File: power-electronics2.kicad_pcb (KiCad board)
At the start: 2 copper layers, 2 parts, among them U1 STP16NF06

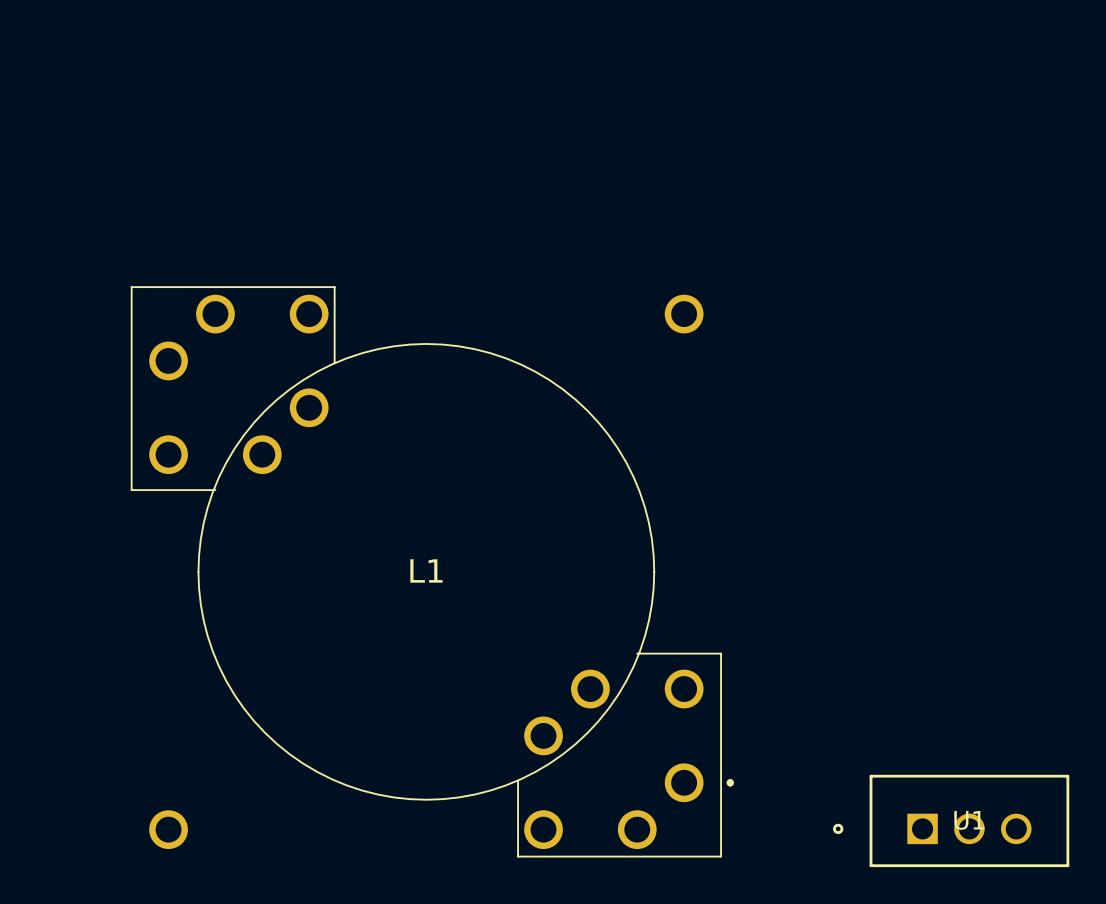
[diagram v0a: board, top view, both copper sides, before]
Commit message: add some components
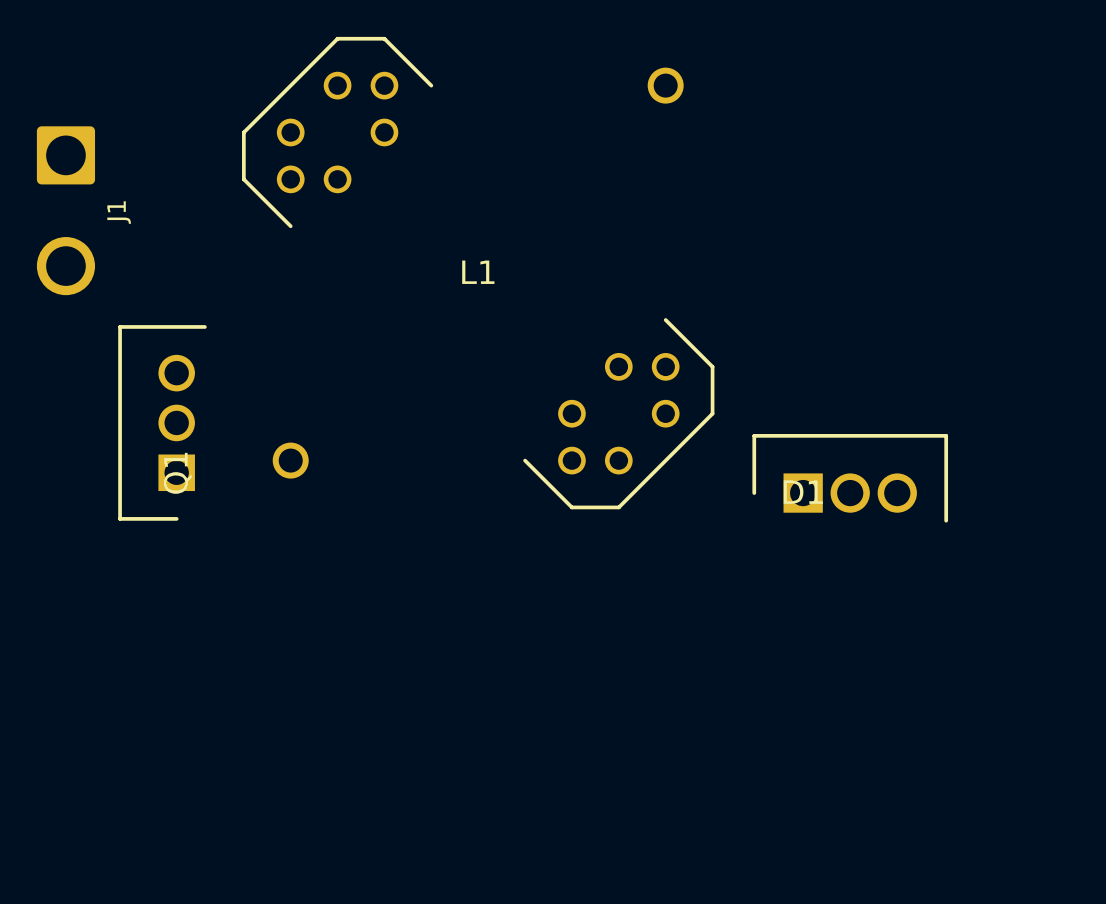
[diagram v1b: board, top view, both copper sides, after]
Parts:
- removed U1: STP16NF06, Snapeda:TO-220_STM
- added D1: STPS10L60CFP, Samacsys:TO255P460X1020X2030-3P, F.Cu at (109.0, 62.3)
- added J1: Vin, Connector_Wire:SolderWire-1.5sqmm_1x02_P6mm_D1.7mm_OD3mm, F.Cu at (69.0, 44.0)
- added Q1: STP16NF06, Samacsys:TO270P460X1020X2008-3P, F.Cu at (75.0, 61.2)
- L1: value B65816N1012D001 -> B65814N1012D001; footprint Samacsys:B65816N1012D001 -> Samacsys:B65814N1012D001
- moved L1 41.2 mm to (81.2, 42.8)
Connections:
- L1 pad 1: unconnected-(L1-Pad1) -> Net-(J1-Pin_1)
- L1 pad 4: unconnected-(L1-Pad4) -> Net-(Q1-D)
- L1 pad 6: unconnected-(L1-Pad6) -> GND
- L1 pad 9: unconnected-(L1-Pad9) -> Net-(D1-A1)

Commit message: add components
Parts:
- added IC1: UC2843BD1, Samacsys:SOIC127P600X175-8M, F.Cu at (59.0, 60.5)
- added IC2: ZTL431AFFTA, Samacsys:SOTFL95P240X110-3N, F.Cu at (161.4, 105.5)
- added L2: B65816N1012D001, Samacsys:B65816N1012D001, F.Cu at (150.1, 116.1)
- added U1: 4N35, Package_DIP:DIP-6_W7.62mm_SMDSocket_SmallPads, F.Cu at (126.7, 128.5)
- moved D1 64.7 mm to (172.5, 74.5), turned to -90 degrees
- moved L1 51.7 mm to (127.8, 65.3)
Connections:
- L1 pad 10: unconnected-(L1-Pad10) -> Net-(D1-A1)
- L1 pad 3: unconnected-(L1-Pad3) -> Net-(Q1-D)
- L1 pad 6: GND -> unconnected-(L1-Pad6)
- L1 pad 7: unconnected-(L1-Pad7) -> GND
- Q1 pad 1: unconnected-(Q1-G-Pad1) -> Net-(IC1-OUTPUT)
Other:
- board outline added: 150 x 100 mm

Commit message: finish pcb
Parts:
- removed L2: B65816N1012D001, Samacsys:B65816N1012D001
- added C1: 47u, Capacitor_THT:CP_Radial_D10.0mm_P5.00mm, F.Cu at (118.5, 31.1)
- added C10: C, Capacitor_SMD:C_0805_2012Metric_Pad1.18x1.45mm_HandSolder, F.Cu at (110.9, 72.9)
- added C11: 1n8, Capacitor_SMD:C_0805_2012Metric_Pad1.18x1.45mm_HandSolder, F.Cu at (57.2, 64.1)
- added C12: 1n8, Capacitor_SMD:C_0805_2012Metric_Pad1.18x1.45mm_HandSolder, F.Cu at (56.9, 59.4)
- added C13: 1n6, Capacitor_SMD:C_0805_2012Metric_Pad1.18x1.45mm_HandSolder, F.Cu at (55.4, 68.7)
- added C14: 1n, Capacitor_SMD:C_0805_2012Metric_Pad1.18x1.45mm_HandSolder, F.Cu at (52.4, 64.1)
- added C15: u1, Capacitor_SMD:C_0805_2012Metric_Pad1.18x1.45mm_HandSolder, F.Cu at (33.9, 59.1)
- added C16: 22u, Capacitor_SMD:C_0805_2012Metric_Pad1.18x1.45mm_HandSolder, F.Cu at (38.7, 68.8)
- added C2: 3u3, Capacitor_THT:C_Axial_L12.0mm_D7.5mm_P15.00mm_Horizontal, F.Cu at (131.1, 41.1)
- added C3: 47u, Capacitor_THT:CP_Radial_D10.0mm_P5.00mm, F.Cu at (118.6, 49.9)
- added C4: 390u, Capacitor_THT:CP_Radial_D10.0mm_P5.00mm, F.Cu at (42.2, 47.3)
- added C5: 1170u, Capacitor_THT:CP_Radial_D16.0mm_P7.50mm, F.Cu at (71.7, 50.6)
- added C6: C, Capacitor_THT:CP_Radial_D10.0mm_P5.00mm, F.Cu at (42.2, 25.3)
- added C7: C, Capacitor_THT:CP_Radial_D10.0mm_P5.00mm, F.Cu at (42.2, 36.4)
- added C8: C, Capacitor_THT:CP_Radial_D10.0mm_P5.00mm, F.Cu at (71.7, 24.9)
- added C9: C, Capacitor_THT:CP_Radial_D10.0mm_P5.00mm, F.Cu at (71.7, 35.9)
- added D2: 1N4005, Diode_THT:D_DO-41_SOD81_P10.16mm_Horizontal, F.Cu at (47.2, 59.5)
- added G***: LOGO, Samacsys:dtulogo, F.Cu at (68.3, 19.3)
- added G***: LOGO, Samacsys:dtulogo, F.Cu at (26.4, 72.6)
- added H1: B65816C1512T001, Samacsys:B65816C1512T001, F.Cu at (112.3, 23.4)
- added IC4: LM317LD, Samacsys:SOIC127P600X175-8N, F.Cu at (40.4, 60.9)
- added J2: Vo, Connector_Wire:SolderWire-1.5sqmm_1x02_P6mm_D1.7mm_OD3mm, F.Cu at (131.1, 32.8)
- added L3: 123u, Inductor_THT:L_Axial_L29.9mm_D14.0mm_P38.00mm_Horizontal_Vishay_IHA-105, F.Cu at (59.2, 17.4)
- added L4: 470u, Inductor_THT:L_Axial_L29.9mm_D14.0mm_P38.00mm_Horizontal_Vishay_IHA-105, F.Cu at (29.7, 55.4)
- added Q2: 2N3906, Package_TO_SOT_THT:TO-92_Inline, F.Cu at (32.6, 69.1)
- added R1: 445m, Resistor_SMD:R_0805_2012Metric_Pad1.20x1.40mm_HandSolder, F.Cu at (39.7, 55.4)
- added R10: 10k, Resistor_SMD:R_0805_2012Metric_Pad1.20x1.40mm_HandSolder, F.Cu at (62.2, 58.7)
- added R11: 12k3, Resistor_SMD:R_0805_2012Metric_Pad1.20x1.40mm_HandSolder, F.Cu at (82.5, 61.0)
- added R12: 10k, Resistor_SMD:R_0805_2012Metric_Pad1.20x1.40mm_HandSolder, F.Cu at (52.4, 59.6)
- added R13: 2k7, Resistor_SMD:R_0805_2012Metric_Pad1.20x1.40mm_HandSolder, F.Cu at (33.8, 62.9)
- added R14: 240R, Resistor_SMD:R_0805_2012Metric_Pad1.20x1.40mm_HandSolder, F.Cu at (42.9, 66.4)
- added R15: 50k, Resistor_SMD:R_0805_2012Metric_Pad1.20x1.40mm_HandSolder, F.Cu at (42.9, 70.9)
- added R2: R, Resistor_SMD:R_0805_2012Metric_Pad1.20x1.40mm_HandSolder, F.Cu at (115.4, 66.4)
- added R3: R, Resistor_SMD:R_0805_2012Metric_Pad1.20x1.40mm_HandSolder, F.Cu at (115.4, 72.1)
- added R4: R, Resistor_SMD:R_0805_2012Metric_Pad1.20x1.40mm_HandSolder, F.Cu at (110.9, 65.3)
- added R5: 10R, Resistor_SMD:R_0805_2012Metric_Pad1.20x1.40mm_HandSolder, F.Cu at (83.8, 65.8)
- added R6: WSR5R1000FEA, Samacsys:RESM11670X254N, F.Cu at (64.9, 70.1)
- added R7: CRA2512-FZ-R050ELF, Samacsys:RESC6434X90N, F.Cu at (76.1, 67.6)
- added R8: CRA2512-FZ-R050ELF, Samacsys:RESC6434X90N, F.Cu at (76.1, 71.9)
- added R9: 100R, Resistor_SMD:R_0805_2012Metric_Pad1.20x1.40mm_HandSolder, F.Cu at (61.9, 64.0)
- added VR1: PTV09A-4020F-B104, Samacsys:PTV09A4020FB103, F.Cu at (126.0, 66.6)
- moved D1 72.5 mm to (125.1, 19.6), turned to 0 degrees
- moved U1 65.1 mm to (99.9, 69.1), turned to 180 degrees
- moved IC2 61.9 mm to (110.9, 69.7), turned to 180 degrees
- moved L1 48.3 mm to (97.9, 27.3), turned to -45 degrees
- moved J1 48.3 mm to (24.2, 61.9)
- moved Q1 17.9 mm to (90.2, 70.6), turned to 180 degrees
- moved IC1 9.61 mm to (68.4, 62.4), turned to 0 degrees
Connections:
- D1 pad 1: Net-(D1-A1) -> /Vs+
- D1 pad 2: unconnected-(D1-K-Pad2) -> /Vo
- D1 pad 3: Net-(D1-A1) -> /Vs+
- IC1 pad 1: unconnected-(IC1-COMP-Pad1) -> Net-(IC1-COMP)
- IC1 pad 2: unconnected-(IC1-VFB-Pad2) -> Net-(IC1-VFB)
- IC1 pad 3: unconnected-(IC1-ISENSE-Pad3) -> Net-(IC1-ISENSE)
- IC1 pad 4: unconnected-(IC1-RT/CT-Pad4) -> Net-(IC1-RT/CT)
- IC1 pad 7: unconnected-(IC1-VI-Pad7) -> /Vldo
- IC1 pad 8: unconnected-(IC1-VREF-Pad8) -> Net-(IC1-VREF)
- IC2 pad 1: unconnected-(IC2-ANODE-Pad1) -> GND
- IC2 pad 2: unconnected-(IC2-REF-Pad2) -> Net-(IC2-REF)
- IC2 pad 3: unconnected-(IC2-CATHODE-Pad3) -> Net-(IC2-CATHODE)
- J1 pad 1: Net-(J1-Pin_1) -> /Vi
- L1 pad 1: Net-(J1-Pin_1) -> /Vp-
- L1 pad 10: Net-(D1-A1) -> Net-(H1-Pad1)
- L1 pad 11: unconnected-(L1-Pad11) -> /Vs+
- L1 pad 12: unconnected-(L1-Pad12) -> GND
- L1 pad 2: unconnected-(L1-Pad2) -> /Vp+
- L1 pad 3: Net-(Q1-D) -> Net-(H1-Pad6)
- L1 pad 4: Net-(Q1-D) -> Net-(H1-Pad7)
- L1 pad 5: unconnected-(L1-Pad5) -> Net-(H1-Pad8)
- L1 pad 6: unconnected-(L1-Pad6) -> /Vp-
- L1 pad 8: unconnected-(L1-Pad8) -> Net-(H1-Pad11)
- L1 pad 9: Net-(D1-A1) -> Net-(H1-Pad12)
- Q1 pad 1: Net-(IC1-OUTPUT) -> Net-(Q1-G)
- Q1 pad 2: Net-(Q1-D) -> /Vp-
- Q1 pad 3: GNDREF -> Net-(Q1-S)
- U1 pad 1: unconnected-(U1-Pad1) -> Net-(R4-Pad2)
- U1 pad 2: unconnected-(U1-Pad2) -> Net-(IC2-CATHODE)
- U1 pad 4: unconnected-(U1-Pad4) -> GNDREF
- U1 pad 5: unconnected-(U1-Pad5) -> Net-(IC1-VFB)
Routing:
- net /Vo: track 0.00 -> 77.4 mm
- net /Vldo: track 0.00 -> 77.4 mm
- net Net-(C4-Pad1): track 0.00 -> 77.0 mm
- net /Vp+: track 0.00 -> 70.6 mm
- net Net-(IC1-VFB): track 0.00 -> 59.6 mm, vias 0 -> 4
- net /Vp-: track 0.00 -> 53.2 mm
- net GNDREF: track 0.00 -> 42.7 mm, vias 0 -> 18
- net Net-(Q1-S): track 0.00 -> 41.0 mm
- net /Vs+: track 0.00 -> 34.5 mm
- net /Vi: track 0.00 -> 27.9 mm
- net Net-(IC4-ADJ): track 0.00 -> 20.3 mm
- net Net-(IC1-COMP): track 0.00 -> 20.1 mm
- net Net-(IC1-RT/CT): track 0.00 -> 17.7 mm, vias 0 -> 2
- net Net-(D2-A): track 0.00 -> 16.5 mm
- net Net-(IC2-REF): track 0.00 -> 15.1 mm
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- added copper zone on B.Cu, net GND
- added copper zone on B.Cu, net GNDREF
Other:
- board size 150 x 100 mm -> 117.1 x 60.5 mm

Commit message: finishing touches & gerber
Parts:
- Q2: footprint Package_TO_SOT_THT:TO-92_Inline -> Package_TO_SOT_SMD:SOT-23_Handsoldering
- moved Q2 0.87 mm to (33.5, 69.0)
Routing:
- net Net-(D2-A): track 16.5 -> 18.0 mm
- net Net-(R4-Pad2): track 13.9 -> 15.1 mm
- net GNDREF: track 42.7 -> 41.8 mm, vias 18 -> 19
- net Net-(IC4-ADJ): track 20.3 -> 19.5 mm
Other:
- outline, holes or cut-outs redrawn
